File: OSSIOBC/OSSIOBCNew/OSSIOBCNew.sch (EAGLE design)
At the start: 158 parts, among them Q2 NX-3215, U1 PCA9548APWR, U10 MAX6369, U11 OPA4347, U13 SN65HVD11QD, U14 LTC4411, U15 MCP1700_SOT23, U16 DS3231-L, U17 FM24V02-G, U18 TMP101, U19 24LC256-8LEAD, U2 ADG708, U20 LTC4411, U21 SN74LVC8T245PWR, U23 ADXRS450SOIC, U3 MAX890L, U4 OPA4347, U5 MSP430F1611, U6 OPA4347, U7 TPS3838, U8 ADG708, U9 ADR121, X1 ESQ-126-38-G-D, X2 JTAG10PINMINI-H, X3 MOLEX-22-05-7045, X5 P-PAD-S, X6 P-PAD-S

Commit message: schematics renumbered
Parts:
- removed C42: 10uF, LDO Tantal 16V, OSSI:C-TANTAL-A
- removed U23: ADXRS450SOIC, OSSI:ADXRS450SOIC
- added C35: 100nF, OSSI:C0603(1608)
- added U12: TMP101, OSSI:TMP101
- C1: value 1uF -> 100nF
- C13, C14: value 12.5pF -> 100nF
- C20, C22, C23: value 100nF -> 1uF 0805; device OSSI:C0603(1608) -> OSSI:C0805(2012)
- C29: value 1uF 0805 -> 4.7uF, 1210; device OSSI:C0805(2012) -> OSSI:C1206(3216)-GCM31
- C30: value 1uF 0805 -> 10uF,3225; device OSSI:C0805(2012) -> OSSI:C1210(3225)-GCM32
- C31: value 100nF -> 12.5pF
- C32: value 1uF 0805 -> 12.5pF; device OSSI:C0805(2012) -> OSSI:C0603(1608)
- C34: value 10uF, LDO Tantal 16V -> 100nF; device OSSI:C-TANTAL-A -> OSSI:C0603(1608)
- C37: value 10uF,3225 -> 100nF; device OSSI:C1210(3225)-GCM32 -> OSSI:C0603(1608)
- C38: value 4.7uF, 1210 -> 1uF; device OSSI:C1206(3216)-GCM31 -> OSSI:C0603(1608)
- C40, C41: value 100nF -> 10uF, LDO Tantal 16V; device OSSI:C0603(1608) -> OSSI:C-TANTAL-A
- R1: value TBD -> 10k
- R10, R11, R62: value 10k -> 100k
- R12, R13: value 33k -> 100k
- R18, R2, R3, R4, R6, R7, R9: value 100k -> 10k
- R19, R41: value 100k -> 250
- R20, R43: value 100k -> 470k
- R21, R30, R31, R38: value 10k -> 250
- R22, R23, R26, R28, R29: value 250 -> 1.5k
- R27: value 250 -> 100k
- R32: value 250 -> 4.7k
- R33: value 250 -> 470k
- R34: value 4.7k -> 470k
- R35: value 120, DNP -> 33k
- R36, R39, R68, R71: value 10k -> 4.7k
- R37: value 10k -> 120, DNP
- R40: value 10k -> 33k
- R42, R69, R70: value 1.5k -> 4.7k
- R44: value 470k -> 4.7k
- R45: value 4.7k -> 100k
- R46: value 1.5k -> 470k
- R47, R48, R49: value 1.5k -> 100k
- R52, R57: value 4.7k -> 1.5k
- R54: value 1.5k -> 10k
- R56: value 10k -> 1.5k
- R58, R60, R65: value 470k -> 10k
- R59, R61, R8: value 4.7k -> 10k
- R63: value 4.7k -> 250
- R64: value 470k -> 250
- R66: value 4.7k -> 300k
- R67: value 300k -> 10k
- R72, R73: value 10k -> 0
- R74: value 100k -> TBD
- R76, R77: value 0 -> 100k
- U1: value PCA9548APWR -> OPA4347; device OSSI:PCA9548APWR -> OSSI:OPA4347
- U10: value MAX6369 -> ADXRS450SOIC; device OSSI:MAX6369 -> OSSI:ADXRS450SOIC
- U11: value OPA4347 -> FM24V02-G; device OSSI:OPA4347 -> OSSI:FM24V02-G
- U14: value LTC4411 -> PCA9548APWR; device OSSI:LTC4411 -> OSSI:PCA9548APWR
- U15: value MCP1700_SOT23 -> SN74LVC8T245PWR; device OSSI:MCP1700_SOT23 -> OSSI:SN74LVC8T245PWR
- U16: value DS3231-L -> LTC4411; device OSSI:DS3231-L -> OSSI:LTC4411
- U17: value FM24V02-G -> MSP430F1611; device OSSI:FM24V02-G -> OSSI:MSP430F1611
- U18: value TMP101 -> MAX6369; device OSSI:TMP101 -> OSSI:MAX6369
- U19: value 24LC256-8LEAD -> TPS3838; device OSSI:24LC256-8LEAD -> OSSI:TPS3838
- U20: value LTC4411 -> MAX890L; device OSSI:LTC4411 -> OSSI:MAX890L
- U21: value SN74LVC8T245PWR -> MCP1700_SOT23; device OSSI:SN74LVC8T245PWR -> OSSI:MCP1700_SOT23
- U3: value MAX890L -> OPA4347; device OSSI:MAX890L -> OSSI:OPA4347
- U4: value OPA4347 -> ADR121; device OSSI:OPA4347 -> OSSI:ADR127BUJZ-REEL7
- U5: value MSP430F1611 -> ADG708; device OSSI:MSP430F1611 -> OSSI:ADG708
- U7: value TPS3838 -> DS3231-L; device OSSI:TPS3838 -> OSSI:DS3231-L
- U8: value ADG708 -> 24LC256-8LEAD; device OSSI:ADG708 -> OSSI:24LC256-8LEAD
- U9: value ADR121 -> LTC4411; device OSSI:ADR127BUJZ-REEL7 -> OSSI:LTC4411
- X2: value JTAG10PINMINI-H -> MOLEX-22-05-7045; device OSSI:JTAG10PINMINI-H -> OSSI:MOLEX-22-05-7045
- X3: value MOLEX-22-05-7045 -> (none); device OSSI:MOLEX-22-05-7045 -> OSSI:M03PTH
- X4: value (none) -> P-PAD-S; device OSSI:M03PTH -> OSSI:P-PAD-S
- X6: value P-PAD-S -> JTAG10PINMINI-H; device OSSI:P-PAD-S -> OSSI:JTAG10PINMINI-H
- renumbered Q2 to Q1, TR2 to TR1
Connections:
- net /RE: now also R40.1; no longer R12.1
- net 3.3VOBC: now also C14.2, C20.1, C26.1, C34.1, C36.1, C37.1, C4.1, C41.+, C9.1, R34.2, R40.2, R46.2, R48.2, R54.2, R59.2, R65.2, R66.1, R67.2, R77.2, U14.P$24, U15.P$1, U17.1, U17.64, U18.P$4, U18.P$5, U18.P$6, U18.P$8, U19.P$5, U1A.V+, U21.2, U3A.V+, U4.P$3, U5.P$13, U5.P$2, U9.P$1, X6.4; no longer C12.1, C17.2, C2.1, C27.1, C30.1, C42.+, C6.1, C7.1, C8.1, R12.2, R2.2, R30.2, R31.2, R4.2, R44.2, R56.2, R58.2, R67.1, R73.2, U1.P$24, U10.P$4, U10.P$5, U10.P$8, U11A.V+, U14.P$1, U15.2, U21.P$1, U23.P$6, U4A.V+, U5.1, U5.64, U7.P$5, U8.P$13, U8.P$2, U9.P$3, X2.4
- net 3.3VOBC_I2C: now also C24.1, C25.1, R20.2, R33.1, R58.2, R61.2, U11.A0, U11.VDD, U12.4, U7.P$2, U8.P$8, U9.P$5; no longer C20.1, C21.1, R5.2, R64.2, R65.1, R72.2, U14.P$5, U16.P$2, U17.A0, U17.VDD, U18.4, U19.P$8
- net A: now also R37.2, X2.2; no longer R35.2, X3.2
- net ADC0: now also C12.1, R9.1, U17.59; no longer C5.1, R10.1, U5.59
- net ADC1: now also C17.1, R18.1, U17.60; no longer C9.1, R11.1, U5.60
- net ANT_DEPLOY1: now also R70.1; no longer R45.1
- net ANT_DEPLOY2: now also R69.1; no longer R52.1
- net B: now also R37.1, X2.3; no longer R35.1, X3.3
- net BAT_-CHRG: now also U15.P$18; no longer U21.P$18
- net BAT_-CHRG_IN: now also R53.2, U17.17; no longer R48.2, U5.17
- net BAT_-FAULT: now also U15.P$17; no longer U21.P$17
- net BAT_-FAULT_IN: now also R52.2, U17.16; no longer R49.2, U5.16
- net BAT_-ON: now also U15.P$20; no longer U21.P$20
- net BAT_-ON_IN: now also R56.2, U17.19; no longer R46.2, U5.19
- net BAT_TEMP: now also R2.2; no longer R68.2
- net BEACON_-FAULT: now also R42.1, R43.1; no longer R58.1, R59.1
- net BEACON_-FAULT_IN: now also R42.2, U17.22; no longer R59.2, U5.22
- net BEACON_OFF: now also R28.1; no longer R54.1
- net BEACON_OFF_OUT: now also R28.2, U17.38; no longer R54.2, U5.38
- net BEACON_SCL: now also U14.P$7; no longer U1.P$7
- net BEACON_SDA: now also U14.P$6; no longer U1.P$6
- net BUS_CS: now also R4.2; no longer R40.2
- net COMMS_-FAULT: now also R32.1, R34.1; no longer R60.1, R61.1
- net COMMS_-FAULT_IN: now also R32.2, U17.21; no longer R61.2, U5.21
- net COMMS_OFF: now also R26.1; no longer R55.1
- net COMMS_OFF_OUT: now also R26.2, U17.37; no longer R55.2, U5.37
- net COMMS_SCL: now also U14.P$5; no longer U1.P$5
- net COMMS_SDA: now also U14.P$4; no longer U1.P$4
- net DE: now also R35.2, U17.48; no longer R13.2, U5.48
- net GND: now also C13.1, C14.1, C17.2, C21.1, C31.2, C33.2, C34.2, C35.2, C40.-, R10.1, R12.1, R14.1, R16.1, R27.2, R35.1, R45.2, R49.2, R74.1, R76.1, U10.P$10, U10.P$11, U10.P$12, U10.P$13, U10.P$3, U10.P$7, U11.A1, U11.A2, U11.VSS, U11.WP, U12.2, U12.5, U14.P$1, U14.P$12, U14.P$21, U15.P$11, U15.P$12, U15.P$13, U15.P$14, U15.P$2, U16.P$2, U17.11, U17.53, U17.62, U17.63, U18.P$2, U1A.V-, U20.P$4, U21.1, U3A.V-, U4.P$2, U5.P$10, U5.P$11, U5.P$12, U5.P$14, U5.P$3, U5.P$9, U7.P$10, U7.P$11, U7.P$12, U7.P$13, U7.P$5, U7.P$6, U7.P$7, U7.P$8, U7.P$9, U8.P$1, U8.P$2, U8.P$4, U8.P$7, X2.4, X3.3, X6.9; no longer C13.2, C14.2, C17.1, C21.2, C31.1, C33.1, C34.-, C40.2, C41.2, R1.1, R13.1, R15.1, R17.1, R19.1, R20.2, R3.1, R41.2, R74.2, R9.1, U1.P$1, U1.P$12, U1.P$2, U1.P$21, U11A.V-, U15.1, U16.P$10, U16.P$11, U16.P$12, U16.P$13, U16.P$5, U16.P$6, U16.P$7, U16.P$8, U16.P$9, U17.A1, U17.A2, U17.VSS, U17.WP, U18.2, U18.5, U19.P$3, U19.P$4, U19.P$7, U2.P$10, U2.P$11, U2.P$12, U2.P$9, U20.P$2, U21.P$11, U21.P$12, U21.P$13, U21.P$14, U21.P$2, U23.P$10, U23.P$11, U23.P$12, U23.P$13, U23.P$2, U23.P$3, U23.P$7, U3.P$4, U4A.V-, U5.11, U5.53, U5.62, U5.63, U7.P$1, U7.P$2, U8.P$14, X2.9, X3.4, X4.3
- net GYRO_-CS: now also U10.P$4, U17.44; no longer U23.P$4, U5.44
- net GYRO_SCLK: now also U10.P$16, U17.47; no longer U23.P$16, U5.47
- net GYRO_SI: now also U10.P$15, U17.45; no longer U23.P$15, U5.45
- net GYRO_SO: now also U10.P$5, U17.46; no longer U23.P$5, U5.46
- net I2C_-RST: now also R48.1, U14.P$3, U17.28; no longer R4.1, U1.P$3, U5.28
- net I2C_SCL: now also R64.1, R67.1, U14.P$22; no longer R26.1, R30.1, U1.P$22
- net I2C_SCL_TP: now also R64.2, U17.31, X3.2; no longer R26.2, U5.31, X4.2
- net I2C_SDA: now also R63.1, R65.1, U14.P$23; no longer R27.1, R31.1, U1.P$23
- net I2C_SDA_TP: now also R63.2, U17.29, X3.1; no longer R27.2, U5.29, X4.1
- net IO_-OE: now also R62.1, U15.P$22, U17.24; no longer R43.1, U21.P$22, U5.24
- net LED_-FAULT: now also R46.1; no longer R57.1
- net LED_-FAULT_IN: now also R44.2, U17.23; no longer R57.2, U5.23
- net LED_OFF: now also R29.1; no longer R53.1
- net LED_OFF_OUT: now also R29.2, U17.39; no longer R53.2, U5.39
- net LED_SCL: now also U14.P$9; no longer U1.P$9
- net LED_SDA: now also U14.P$8; no longer U1.P$8
- net MUX_A0: now also R73.2, U5.P$1; no longer R76.2, U8.P$1
- net MUX_A1: now also R72.2, U5.P$16; no longer R77.2, U8.P$16
- net MUX_A2: now also U17.51, U5.P$15; no longer U5.51, U8.P$15
- net N$1: now also U17.12, U18.P$1; no longer U10.P$1, U5.12
- net N$10: now also R74.2, U20.P$5; no longer R1.2, U3.P$5
- net N$11: now also U5.P$4, U6D.-IN, U6D.OUT; no longer U2.P$4, U4D.-IN, U4D.OUT
- net N$12: now also U2.P$7, U3A.-IN, U3A.OUT; no longer U6A.-IN, U6A.OUT, U8.P$7
- net N$13: now also C33.1, U17.7; no longer C10.1, U5.7
- net N$14: now also R39.2; no longer R34.2
- net N$15: now also R21.2, U7.P$16; no longer R33.2, U16.P$16
- net N$16: now also R54.1, U14.P$15, U14.P$16, U14.P$17, U14.P$18, U14.P$19, U14.P$20; no longer R73.1, U1.P$15, U1.P$16, U1.P$17, U1.P$18, U1.P$19, U1.P$20
- net N$17: now also U17.57, X6.7; no longer U5.57, X2.7
- net N$18: now also U17.56, X6.5; no longer U5.56, X2.5
- net N$19: now also U17.55, X6.3; no longer U5.55, X2.3
- net N$2: now also R16.2, R17.1, U6A.+IN; no longer R7.1, R9.2, U4A.+IN
- net N$20: now also U17.54, X6.1; no longer U5.54, X2.1
- net N$21: now also U2.P$6, U3B.-IN, U3B.OUT; no longer U6B.-IN, U6B.OUT, U8.P$6
- net N$22: now also R36.2; no longer R63.2
- net N$23: now also R71.1, X6.10; no longer R8.1, X2.10
- net N$24: now also R14.2, R15.1, U6B.+IN; no longer R14.1, R15.2, U4B.+IN
- net N$25: now also R12.2, R13.1, U6C.+IN; no longer R16.1, R17.2, U4C.+IN
- net N$26: now also R10.2, R11.1, U6D.+IN; no longer R18.1, R19.2, U4D.+IN
- net N$27: now also R18.2, U5.P$8; no longer R11.2, U2.P$8
- net N$28: now also U2.P$5, U3C.-IN, U3C.OUT; no longer U6C.-IN, U6C.OUT, U8.P$5
- net N$29: now also R9.2, U2.P$8; no longer R10.2, U8.P$8
- net N$3: now also U5.P$7, U6A.-IN, U6A.OUT; no longer U2.P$7, U4A.-IN, U4A.OUT
- net N$30: now also U2.P$4, U3D.-IN, U3D.OUT; no longer U6D.-IN, U6D.OUT, U8.P$4
- net N$31: now also U1A.-IN, U1A.OUT, U2.P$12; no longer U11A.-IN, U11A.OUT, U8.P$12
- net N$32: now also R68.2, U17.13; no longer R66.2, U5.13
- net N$33: now also C23.1, U10.P$1; no longer C32.1, U23.P$1
- net N$34: now also R24.2, U8.P$5; no longer R29.2, U19.P$5
- net N$35: now also R25.2, U8.P$6; no longer R28.2, U19.P$6
- net N$36: now also R30.2, U11.SDA; no longer R25.2, U17.SDA
- net N$37: now also R70.2, U17.43; no longer R45.2, U5.43
- net N$38: now also R69.2, U17.42; no longer R52.2, U5.42
- net N$39: now also R31.2, U11.SCL; no longer R24.2, U17.SCL
- net N$4: now also R45.1, R47.2; no longer R41.1, R6.2
- net N$40: now also R38.2, U12.6; no longer R22.2, U18.6
- net N$41: now also R41.2, U12.1; no longer R23.2, U18.1
- net N$42: now also R66.2, U17.25; no longer R67.2, U5.25
- net N$43: now also C27.1, X2.1; no longer C36.1, X3.1
- net N$44: now also U1C.-IN, U1C.OUT, U2.P$10; no longer U11C.-IN, U11C.OUT, U8.P$10
- net N$45: now also U1D.-IN, U1D.OUT, U2.P$9; no longer U11D.-IN, U11D.OUT, U8.P$9
- net N$46: now also C22.1, U10.P$14; no longer C29.1, U23.P$14
- net N$47: now also C1.1, R1.1, U1D.+IN; no longer C41.1, R71.1, U11D.+IN
- net N$48: now also C2.1, R2.1, U1C.+IN; no longer C40.1, R68.1, U11C.+IN
- net N$49: now also R53.1, U15.P$6; no longer R48.1, U21.P$6
- net N$5: now also C32.1, U17.8; no longer C13.1, U5.8
- net N$50: now also R52.1, U15.P$7; no longer R49.1, U21.P$7
- net N$51: now also C10.1, R8.1, U3A.+IN; no longer C22.1, R21.1, U6A.+IN
- net N$52: now also C8.1, R7.1, U3B.+IN; no longer C23.1, R36.1, U6B.+IN
- net N$53: now also C7.1, R6.1, U3C.+IN; no longer C24.1, R37.1, U6C.+IN
- net N$54: now also C6.1, R5.1, U3D.+IN; no longer C25.1, R38.1, U6D.+IN
- net N$55: now also C3.1, R3.1, U1A.+IN; no longer C26.1, R39.1, U11A.+IN
- net N$56: now also R51.1, U15.P$8; no longer R50.1, U21.P$8
- net N$57: now also R50.1, U15.P$9; no longer R51.1, U21.P$9
- net N$58: now also C5.1, R4.1, U1B.+IN; no longer C39.1, R40.1, U11B.+IN
- net N$59: now also C41.-; no longer C42.-
- net N$6: now also C31.1, U17.9; no longer C14.1, U5.9
- net N$60: now also U17.33; no longer U5.33
- net N$61: now also U17.32, X4.P$1; no longer U5.32, X6.P$1
- net N$62: now also R73.1, U17.49; no longer R76.1, U5.49
- net N$64: now also R72.1, U17.50; no longer R77.1, U5.50
- net N$65: now also U7.P$14; no longer U16.P$14
- net N$666: now also C39.1, C40.+, U20.P$6, U20.P$7, U21.3; no longer C3.1, C34.+, U15.3, U3.P$6, U3.P$7
- net N$7: now also R19.2, U7.P$15; no longer R32.2, U16.P$15
- net N$70: now also R55.1, U15.P$5; no longer R47.1, U21.P$5
- net N$71: now also R56.1, U15.P$4; no longer R46.1, U21.P$4
- net N$72: now also R57.1, U15.P$3; no longer R42.1, U21.P$3
- net N$8: now also U5.P$6, U6B.-IN, U6B.OUT; no longer U2.P$6, U4B.-IN, U4B.OUT
- net N$82: now also U10.P$8; no longer U23.P$8
- net N$9: now also U5.P$5, U6C.-IN, U6C.OUT; no longer U2.P$5, U4C.-IN, U4C.OUT
- net N$90: now also C21.2, U10.P$9; no longer C31.2, U23.P$9
- net OBC_-FAULT: now also U20.P$8; no longer U3.P$8
- net OBC_I2C_OFF: now also R27.1, U17.30, U9.P$3; no longer R74.1, U14.P$3, U5.30
- net OBC_OFF: now also C38.1, R76.2, U20.P$3; no longer C1.1, R3.2, U3.P$3
- net OBC_SCL: now also R21.1, R25.1, R31.1, R41.1, R58.1, U14.P$14; no longer R23.1, R24.1, R28.1, R33.1, R72.1, U1.P$14
- net OBC_SDA: now also R19.1, R24.1, R30.1, R38.1, R61.1, U14.P$13; no longer R22.1, R25.1, R29.1, R32.1, R5.1, U1.P$13
- net OBC_WT_RST: now also C35.1, U18.P$7, U19.P$3; no longer C4.1, U10.P$7, U7.P$3
- net PANELTEMP_SCL: now also R59.1, U14.P$11; no longer R56.1, U1.P$11
- net PANELTEMP_SDA: now also R60.1, U14.P$10; no longer R62.1, U1.P$10
- net RESETOBC: now also R71.2, R77.1, U17.58, U19.P$4; no longer R2.1, R8.2, U5.58, U7.P$4
- net RTC_-INT: now also R20.1, U17.26, U7.P$3; no longer R64.1, U16.P$3, U5.26
- net RXD1: now also R39.1, U17.35; no longer R34.1, U5.35
- net SCCHG_EN: now also R23.1; no longer R69.1
- net SCCHG_EN_OUT: now also R23.2, U17.41; no longer R69.2, U5.41
- net SCOUT_-PG: now also U15.P$15; no longer U21.P$15
- net SCOUT_-PG_IN: now also R50.2, U17.14; no longer R51.2, U5.14
- net SCOUT_EN: now also R22.1; no longer R70.1
- net SCOUT_EN_OUT: now also R22.2, U17.40; no longer R70.2, U5.40
- net SC_-ON: now also U15.P$19; no longer U21.P$19
- net SC_-ON_IN: now also R55.2, U17.18; no longer R47.2, U5.18
- net SC_-PFO: now also U15.P$16; no longer U21.P$16
- net SC_-PFO_IN: now also R51.2, U17.15; no longer R50.2, U5.15
- net SOLAR_-ON: now also U15.P$21; no longer U21.P$21
- net SOLAR_-ON_IN: now also R57.2, U17.20; no longer R42.2, U5.20
- net SOLAR_CS1: now also R8.2; no longer R21.2
- net SOLAR_CS2: now also R7.2; no longer R36.2
- net SOLAR_CS3: now also R6.2; no longer R37.2
- net SOLAR_CS4: now also R5.2; no longer R38.2
- net SOLAR_CS5: now also R3.2; no longer R39.2
- net STATUS_LED: now also R68.1; no longer R66.1
- net SUN_IN: now also U1B.-IN, U1B.OUT, U2.P$11; no longer U11B.-IN, U11B.OUT, U8.P$11
- net SUPERCAP_TEMP: now also R1.2; no longer R71.2
- net TEMP_-ALERT: now also R33.2, U12.3, U17.27; no longer R65.2, U18.3, U5.27
- net TXD1: now also R36.1, U17.34; no longer R63.1, U5.34
- net VBAT: now also R13.2; no longer R16.2
- net VBUS: now also R15.2, U15.P$23, U15.P$24, U20.P$1, U20.P$2; no longer R14.2, U21.P$23, U21.P$24, U3.P$1, U3.P$2
- net VEXT: now also C30.1, R47.1, U16.P$1; no longer C37.1, R6.1, U20.P$1
- net VEXT_OFF: now also R49.1, U16.P$3, U17.36; no longer R20.1, U20.P$3, U5.36
- net VREF_EXT: now also C13.2, U17.10, U4.P$4; no longer C33.2, U5.10, U9.P$4
- net VSOLAR: now also C29.1, R17.2, U16.P$5; no longer C38.1, R7.2, U20.P$5
- net VSUPERCAP: now also R11.2; no longer R18.2

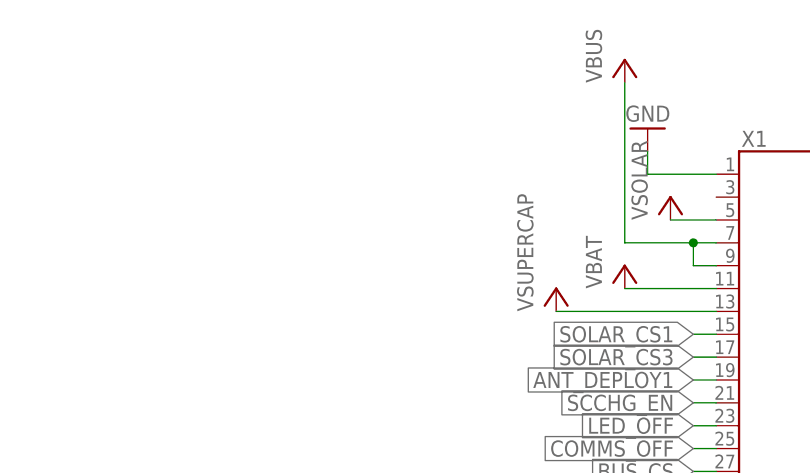
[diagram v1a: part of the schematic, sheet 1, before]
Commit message: OBC renumbered
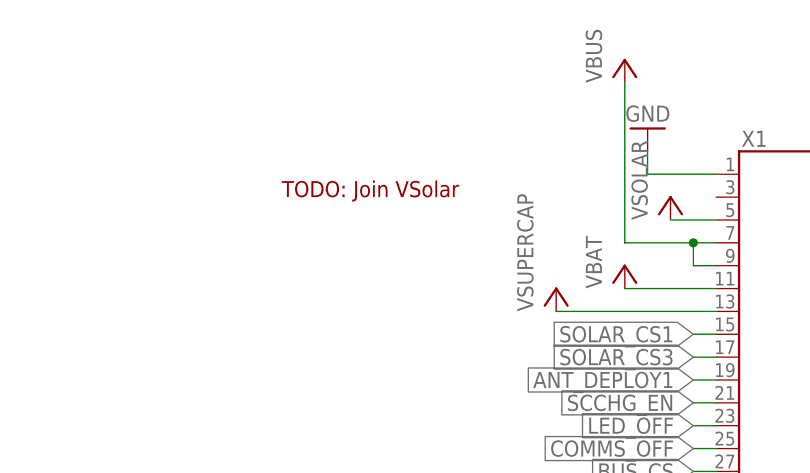
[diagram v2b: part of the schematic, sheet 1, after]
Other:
- note added: "TODO: Join VSolar"
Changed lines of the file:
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@@
 <sheet>
 <plain>
+<text x="144.78" y="172.72" size="1.778" layer="94">TODO: Join VSolar</text>
 </plain>
 <instances>

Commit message: all values for tuned results are updated
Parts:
- R74: value TBD -> 6.2k
- U14: value PCA9548APWR -> TCA9548APWR
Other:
- note added: "/CS pulled up"
- note added: "222.5mA limit"
- note added: "Short warning! modify layout!!!"
- note added: "This section needs pullup resistor as the other sides are pulled up!!!"
- note added: "same conditon for both sides!"
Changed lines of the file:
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@@
 <part name="U20" library="OSSI" deviceset="MAX890L" device=""/>
 <part name="GND1" library="OSSI" deviceset="GND" device=""/>
-<part name="R74" library="OSSI" deviceset="R" device="0603(1608)" value="TBD"/>
+<part name="R74" library="OSSI" deviceset="R" device="0603(1608)" value="6.2k"/>
 <part name="GND3" library="OSSI" deviceset="GND" device=""/>
 <part name="VBUS2" library="OSSI" deviceset="VBUS" device=""/>
@@
 <part name="C12" library="OSSI" deviceset="C" device="0603(1608)" value="100nF"/>
 <part name="GND13" library="OSSI" deviceset="GND" device=""/>
-<part name="U14" library="OSSI" deviceset="PCA9548APWR" device=""/>
+<part name="U14" library="OSSI" deviceset="PCA9548APWR" device="" value="TCA9548APWR"/>
 <part name="R48" library="OSSI" deviceset="R" device="0603(1608)" value="100k"/>
 <part name="3.3VOBC8" library="OSSI" deviceset="3.3VOBC" device=""/>
@@
 <text x="5.08" y="177.8" size="1.778" layer="94">VEXT will turn on the 485 in Receiver mode</text>
 <text x="5.08" y="119.38" size="1.778" layer="94">OBC pull high DE pin when TX</text>
+<text x="236.22" y="243.84" size="1.778" layer="94">This section needs pullup resistor as the other sides are pulled up!!! </text>
+<text x="236.22" y="241.3" size="1.778" layer="94">same conditon for both sides!</text>
+<text x="33.02" y="104.14" size="1.778" layer="94">Short warning! modify layout!!!</text>
+<text x="22.86" y="93.98" size="1.778" layer="94">/CS pulled up</text>
 </plain>
 <instances>
@@
 <text x="238.76" y="205.74" size="1.778" layer="94">Remove 0 Ohm for SMCLK / ACLK out</text>
 <text x="208.28" y="40.64" size="1.778" layer="94">ROSC for better DCO</text>
+<text x="86.36" y="203.2" size="1.778" layer="94">222.5mA limit</text>
 </plain>
 <instances>

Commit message: design files are added
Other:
- note added: "SCOUT_-PG is not used"
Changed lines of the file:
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@@
 <?xml version="1.0" encoding="utf-8"?>
 <!DOCTYPE eagle SYSTEM "eagle.dtd">
-<eagle version="6.1">
+<eagle version="6.5.0">
 <drawing>
 <settings>
@@
 <plain>
 <text x="144.78" y="172.72" size="1.778" layer="94">TODO: Join VSolar</text>
+<text x="223.52" y="109.22" size="1.778" layer="94">SCOUT_-PG is not used </text>
 </plain>
 <instances>
